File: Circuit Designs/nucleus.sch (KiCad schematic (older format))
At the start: 69 parts

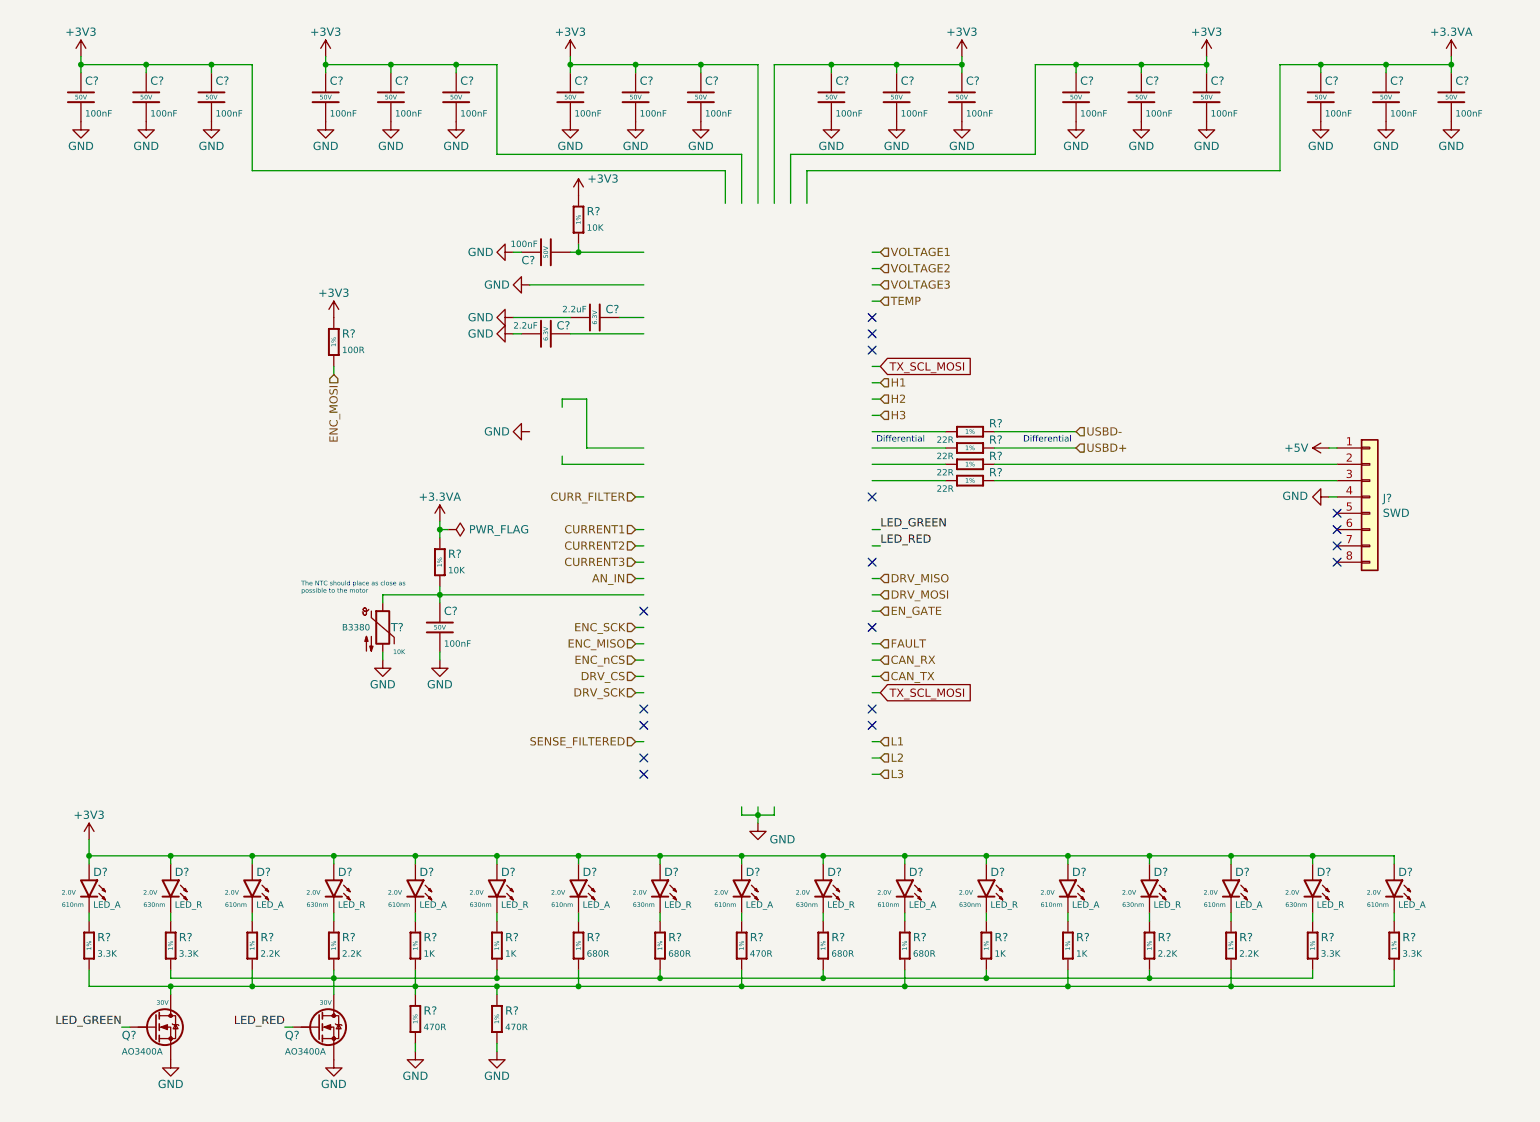
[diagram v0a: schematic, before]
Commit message: added the MCU, duplicated the LEDs for bottom side, changed the can driver to tcan330
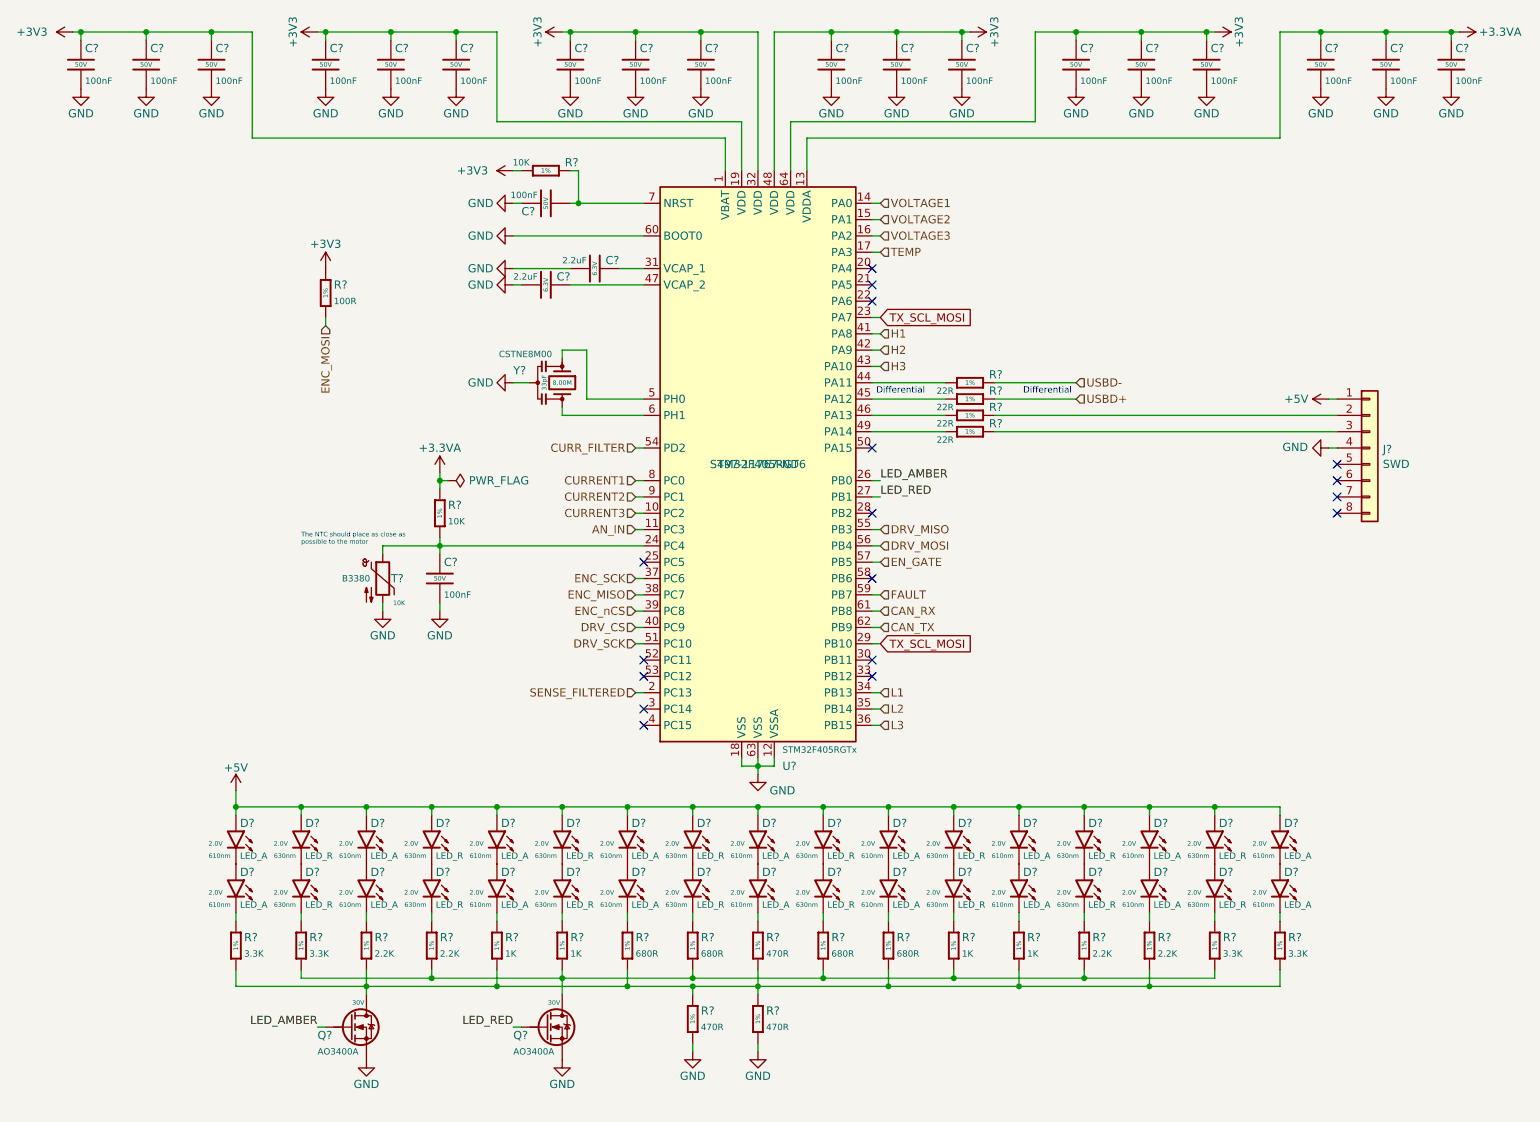
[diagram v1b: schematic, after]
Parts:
- added D? (x8): LED_R, LED_SMD:LED_0603_1608Metric, symbol CoE_Diode:LED_R
- added D? (x9): LED_A, LED_SMD:LED_0603_1608Metric, symbol CoE_Diode:LED_A
- added U?: STM32F405RGTx, Package_QFP:LQFP-64_10x10mm_P0.5mm, symbol CoE_IntegratedCircuit:STM32F405RGTx
- added Y?: CSTNE8M00, symbol CoE_Clock:CSTNE8M00
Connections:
- net labels added: LED_AMBER
- net labels removed: LED_GREEN
- wire segments 222 -> 224
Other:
- moved on the sheet: C?, D?, J?, Q?, R?, T?

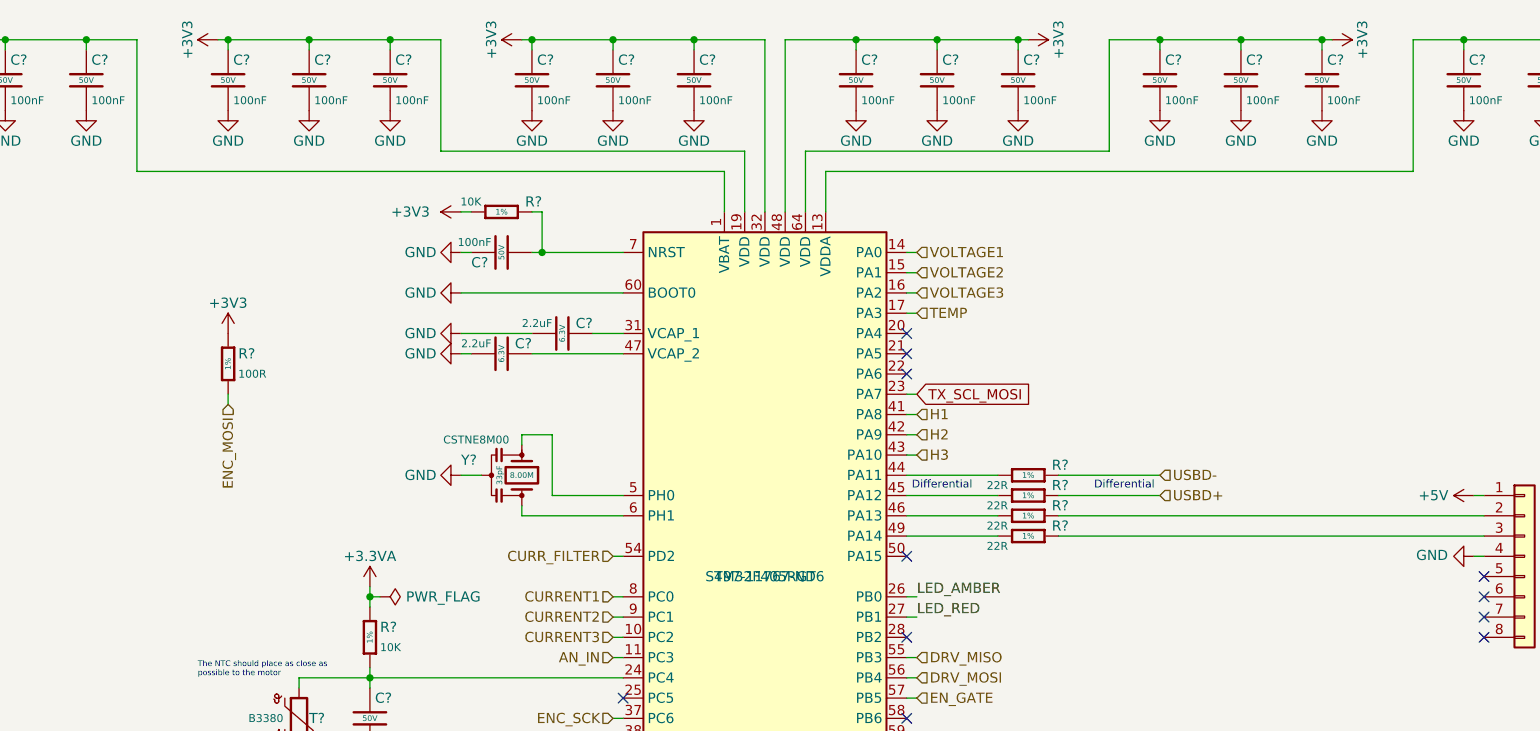
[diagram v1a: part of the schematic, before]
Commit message: added motor driver and adjustable regulators. Now, it is the time to start the detailed review
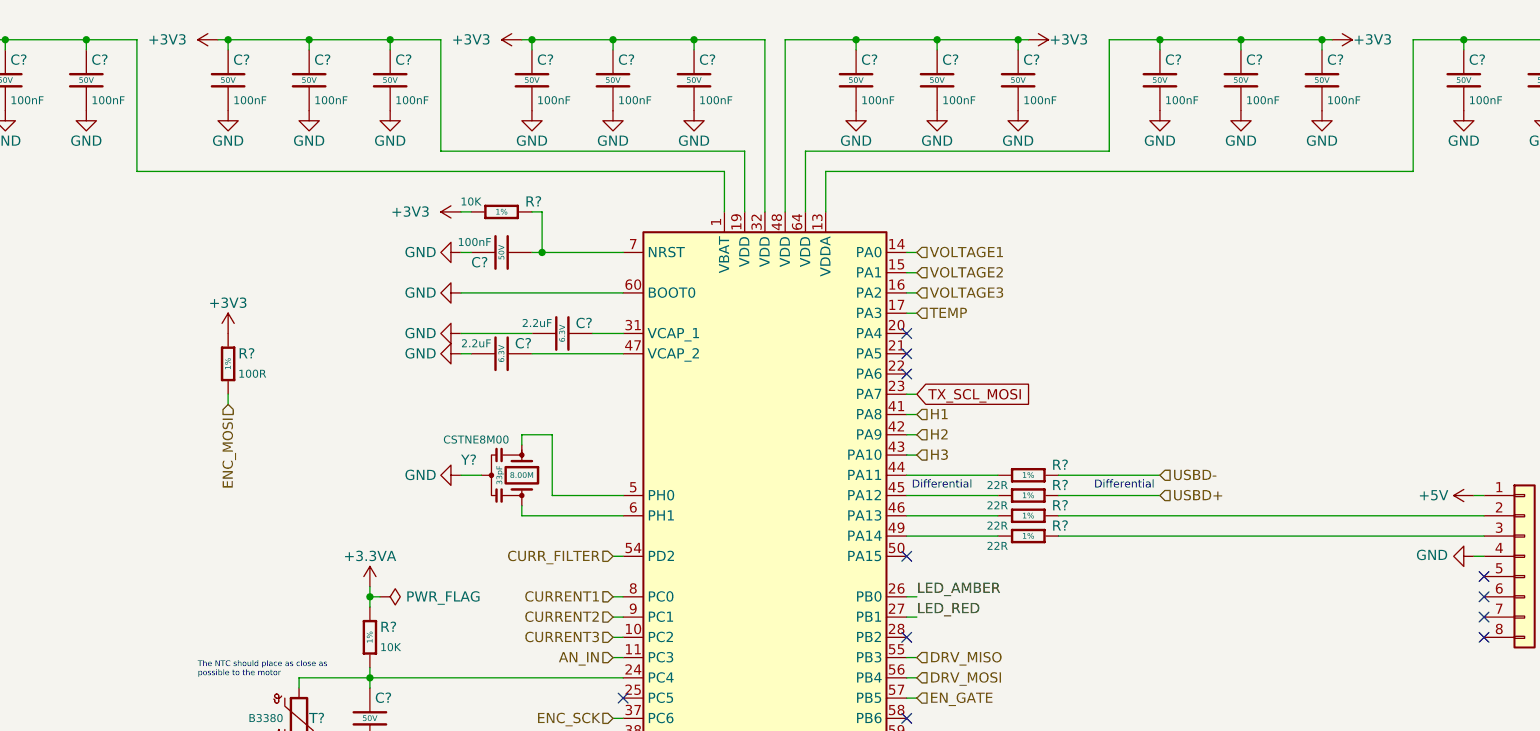
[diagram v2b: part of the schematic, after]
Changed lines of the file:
@@
 P 8750 650
 F 0 "#PWR?" H 8750 500 50  0001 C CNN
-F 1 "+3V3" H 8750 800 50  0000 C CNN
+F 1 "+3V3" V 8750 850 50  0000 C CNN
 F 2 "" H 8750 650 50  0001 C CNN
 F 3 "" H 8750 650 50  0001 C CNN
@@
 P 7250 650
 F 0 "#PWR?" H 7250 500 50  0001 C CNN
-F 1 "+3V3" H 7250 800 50  0000 C CNN
+F 1 "+3V3" V 7250 850 50  0000 C CNN
 F 2 "" H 7250 650 50  0001 C CNN
 F 3 "" H 7250 650 50  0001 C CNN
@@
 P 4750 650
 F 0 "#PWR?" H 4750 500 50  0001 C CNN
-F 1 "+3V3" H 4750 800 50  0000 C CNN
+F 1 "+3V3" V 4750 900 50  0000 C CNN
 F 2 "" H 4750 650 50  0001 C CNN
 F 3 "" H 4750 650 50  0001 C CNN
@@
 P 3250 650
 F 0 "#PWR?" H 3250 500 50  0001 C CNN
-F 1 "+3V3" H 3250 800 50  0000 C CNN
+F 1 "+3V3" V 3250 900 50  0000 C CNN
 F 2 "" H 3250 650 50  0001 C CNN
 F 3 "" H 3250 650 50  0001 C CNN
@@
 F 1 "STM32F405RGTx" H 6100 1550 39  0000 L CNN
 F 2 "Package_QFP:LQFP-64_10x10mm_P0.5mm" H 5950 1050 50  0001 C CNN
-F 3 "http://www.st.com/st-web-ui/static/active/en/resource/technical/document/datasheet/DM00037051.pdf" H 5950 3300 50  0001 C CNN
-F 4 "STM32F405RGT6" H 5950 3300 50  0000 C CNN "MFR. Part #"
-F 5 "497-11767-ND" H 5950 3300 50  0000 C CNN "Digikey Part #"
+F 3 "http://www.st.com/st-web-ui/static/active/en/resource/technical/document/datasheet/DM00037051.pdf" H 5950 650 50  0001 C CNN
+F 4 "STM32F405RGT6" H 5950 950 50  0001 C CNN "MFR. Part #"
+F 5 "497-11767-ND" H 5950 850 50  0001 C CNN "Digikey Part #"
 	1    5950 3300
 	1    0    0    -1

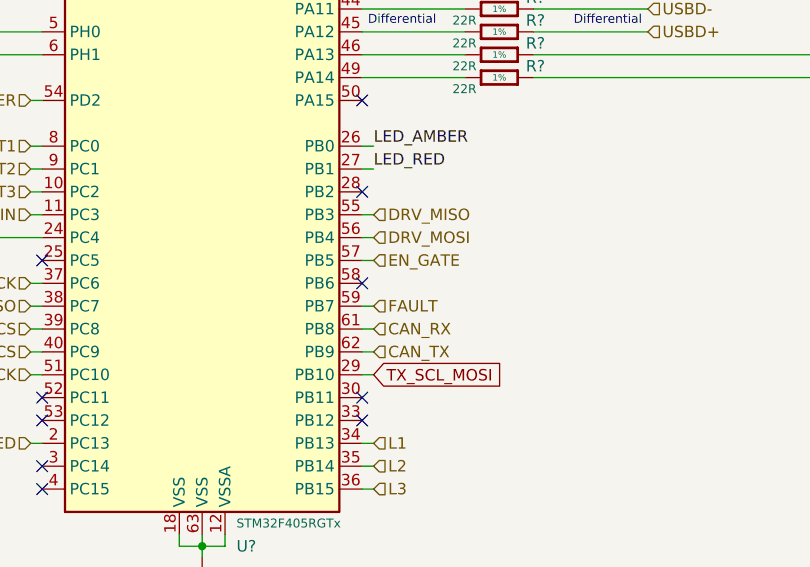
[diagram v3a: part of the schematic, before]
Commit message: added servo control input feature
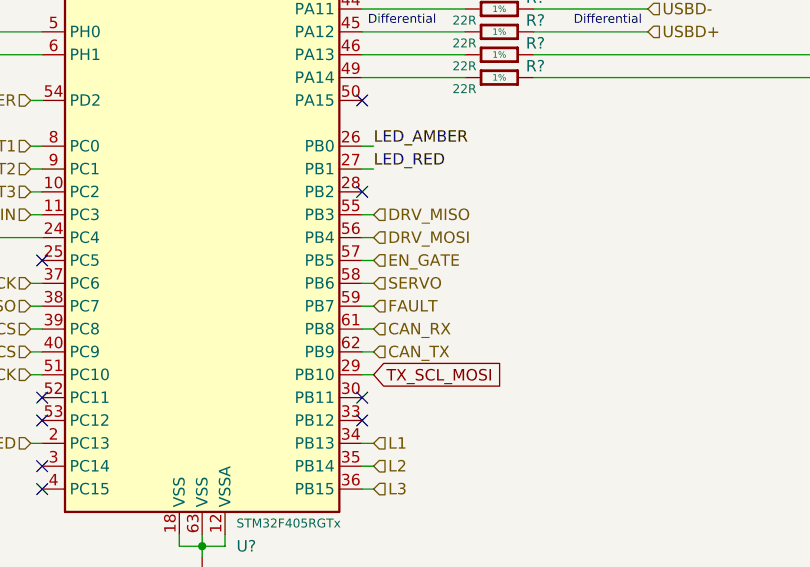
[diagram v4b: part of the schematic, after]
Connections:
- net SERVO: now reaches U?.58 (PB6)
- no-connect marks 17 -> 16
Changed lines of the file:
@@
 Wire Wire Line
 	6700 4100 6650 4100
-NoConn ~ 6650 4000
 Wire Wire Line
 	6700 3900 6650 3900
@@
 Wire Wire Line
 	6250 1500 6250 1300
+Wire Wire Line
+	6700 4000 6650 4000
+Text HLabel 6700 4000 2    50   Input ~ 0
+SERVO
 $EndSCHEMATC
